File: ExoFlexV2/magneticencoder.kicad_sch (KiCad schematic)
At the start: 14 parts

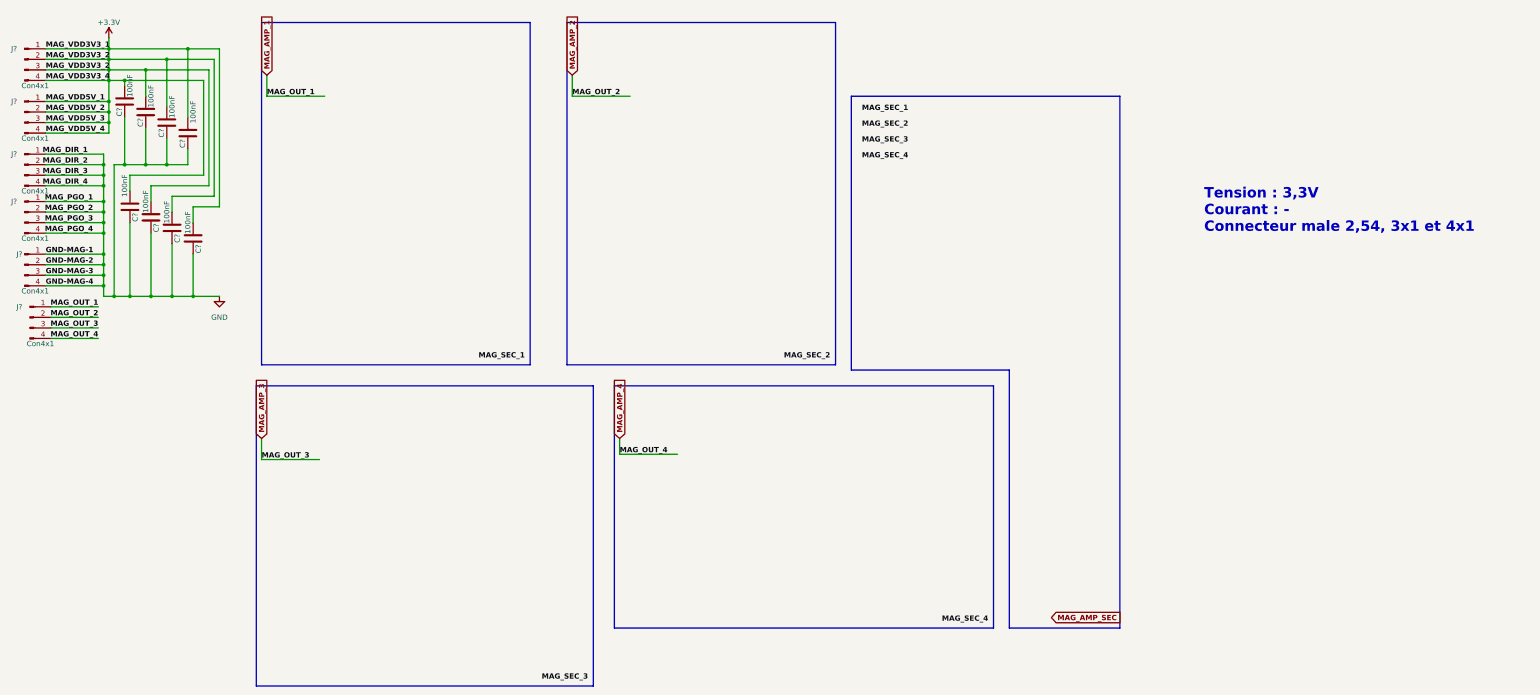
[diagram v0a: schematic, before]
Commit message: Schematic structure
Ajout des Encodeur magnétique et load cells, début de circuit de comparateurs
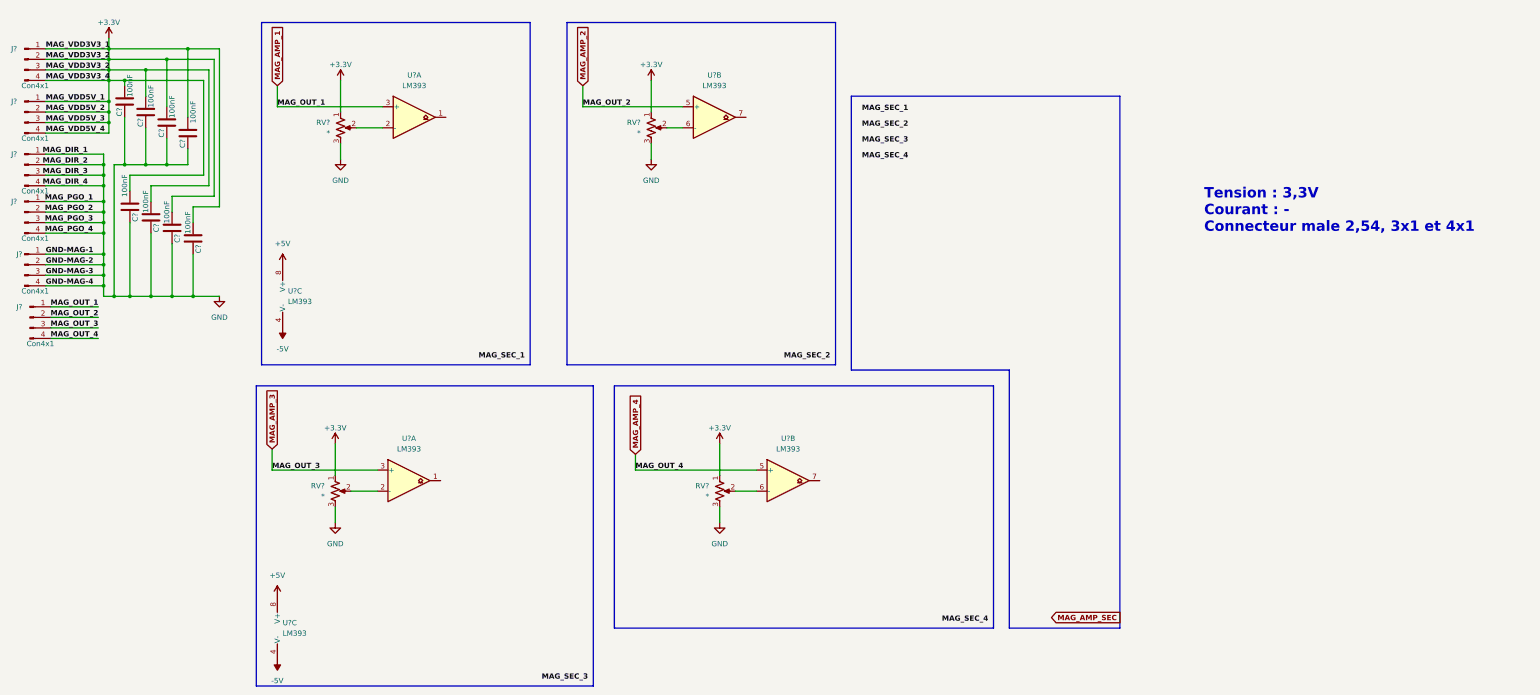
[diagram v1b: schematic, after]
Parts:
- added RV? (x4): *, symbol Device:R_Potentiometer_US
- added U? (x6): LM393, symbol Comparator:LM393
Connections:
- net +3.3V: now also RV?.1, RV?.1, RV?.1, RV?.1
- net GND: now also RV?.3, RV?.3, RV?.3, RV?.3
- net MAG_AMP_1: now also U?.3 (+)
- net MAG_AMP_2: now also U?.5 (+)
- net MAG_AMP_3: now also U?.3 (+)
- net MAG_AMP_4: now also U?.5 (+)
- new net: RV?.2, U?.6 (-) (x2)
- new net: RV?.2, U?.2 (-) (x2)
- new net +5V: U?.8 (V+), U?.8 (V+)
- new net -5V: U?.4 (V-), U?.4 (V-)

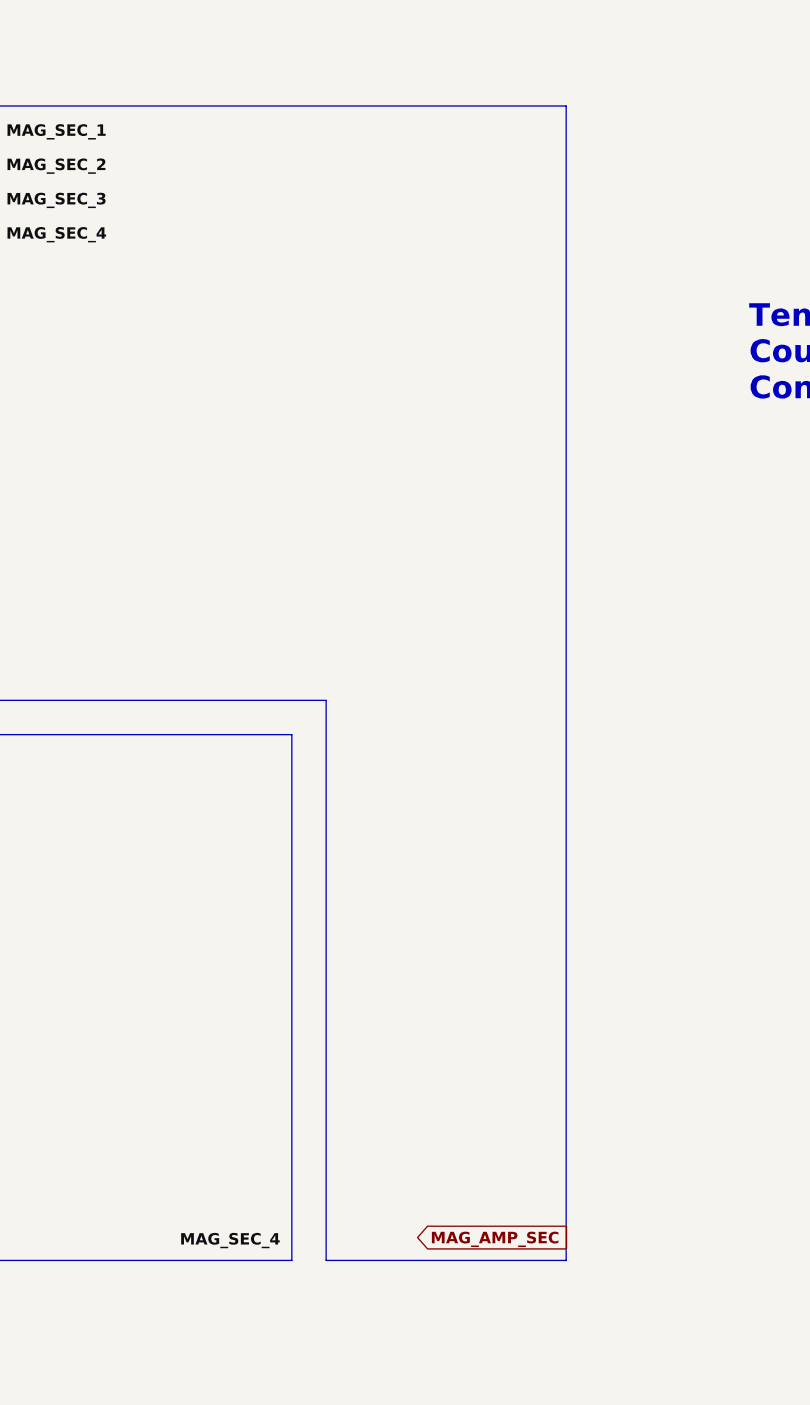
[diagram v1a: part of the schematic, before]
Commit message: Many changes
Debouncing, power protection, potentiometer limits, etc.
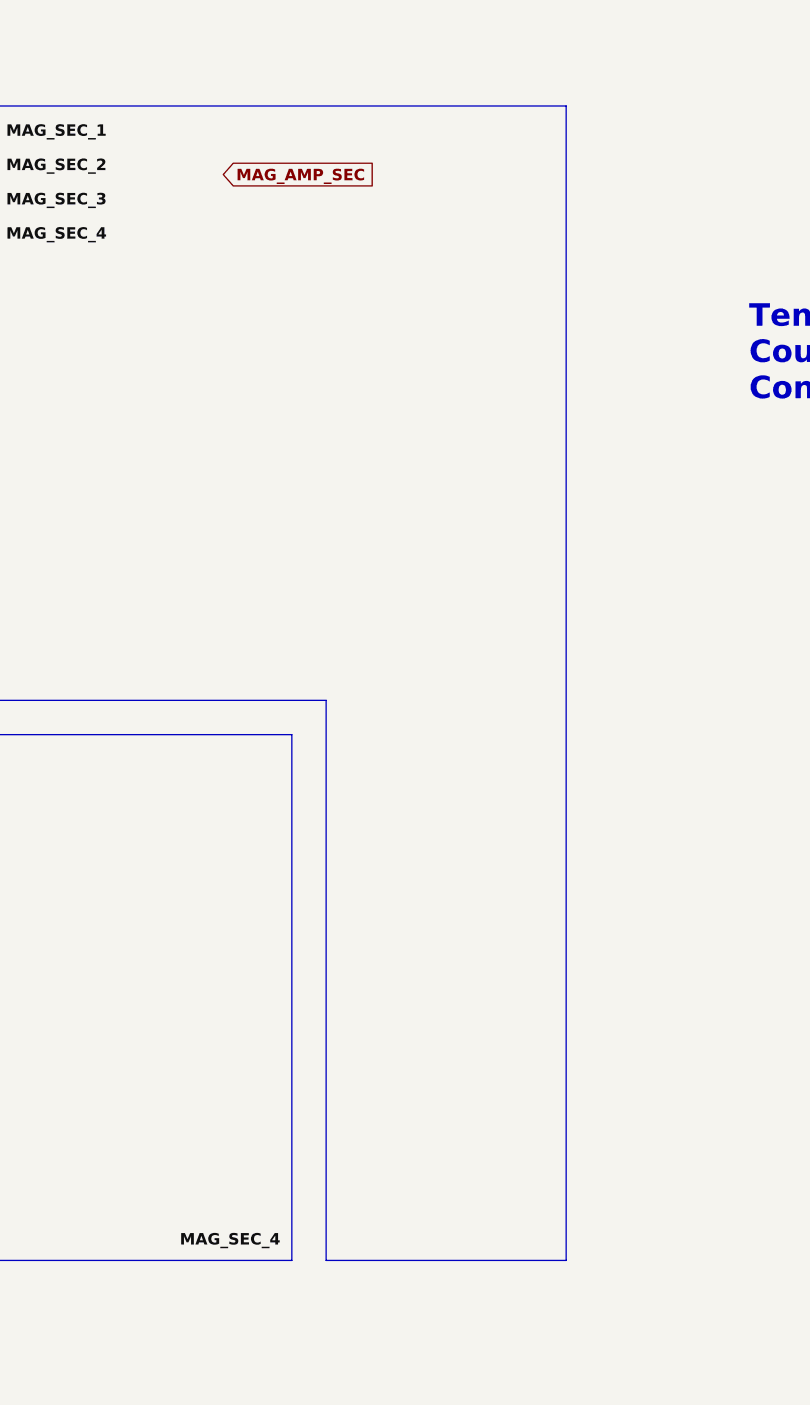
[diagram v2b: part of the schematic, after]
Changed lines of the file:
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@@
     )
   )
-  (global_label "MAG_AMP_SEC" (shape input) (at 266.7 160.02 0) (fields_autoplaced)
+  (global_label "MAG_AMP_SEC" (shape input) (at 245.11 41.91 0) (fields_autoplaced)
     (effects (font (size 1.27 1.27) bold) (justify left))
-    (property "Intersheet References" "${INTERSHEET_REFS}" (id 0) (at 282.6778 159.893 0)
+    (property "Intersheet References" "${INTERSHEET_REFS}" (id 0) (at 261.0878 41.783 0)
       (effects (font (size 1.27 1.27) bold) (justify left) hide)
     )
